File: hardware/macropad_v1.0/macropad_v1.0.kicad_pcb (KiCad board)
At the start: 2 copper layers, 61.9 x 76.2 mm, 50 parts, among them J1 USB_C_Receptacle_USB2.0_14P, SW1 SW_Push, SW2 Rotary Encoder, SW3 Rotary Encoder, U1 USBLC6-2SC6, U2 STM32F072C8T6, U3 XC6206PxxxMR

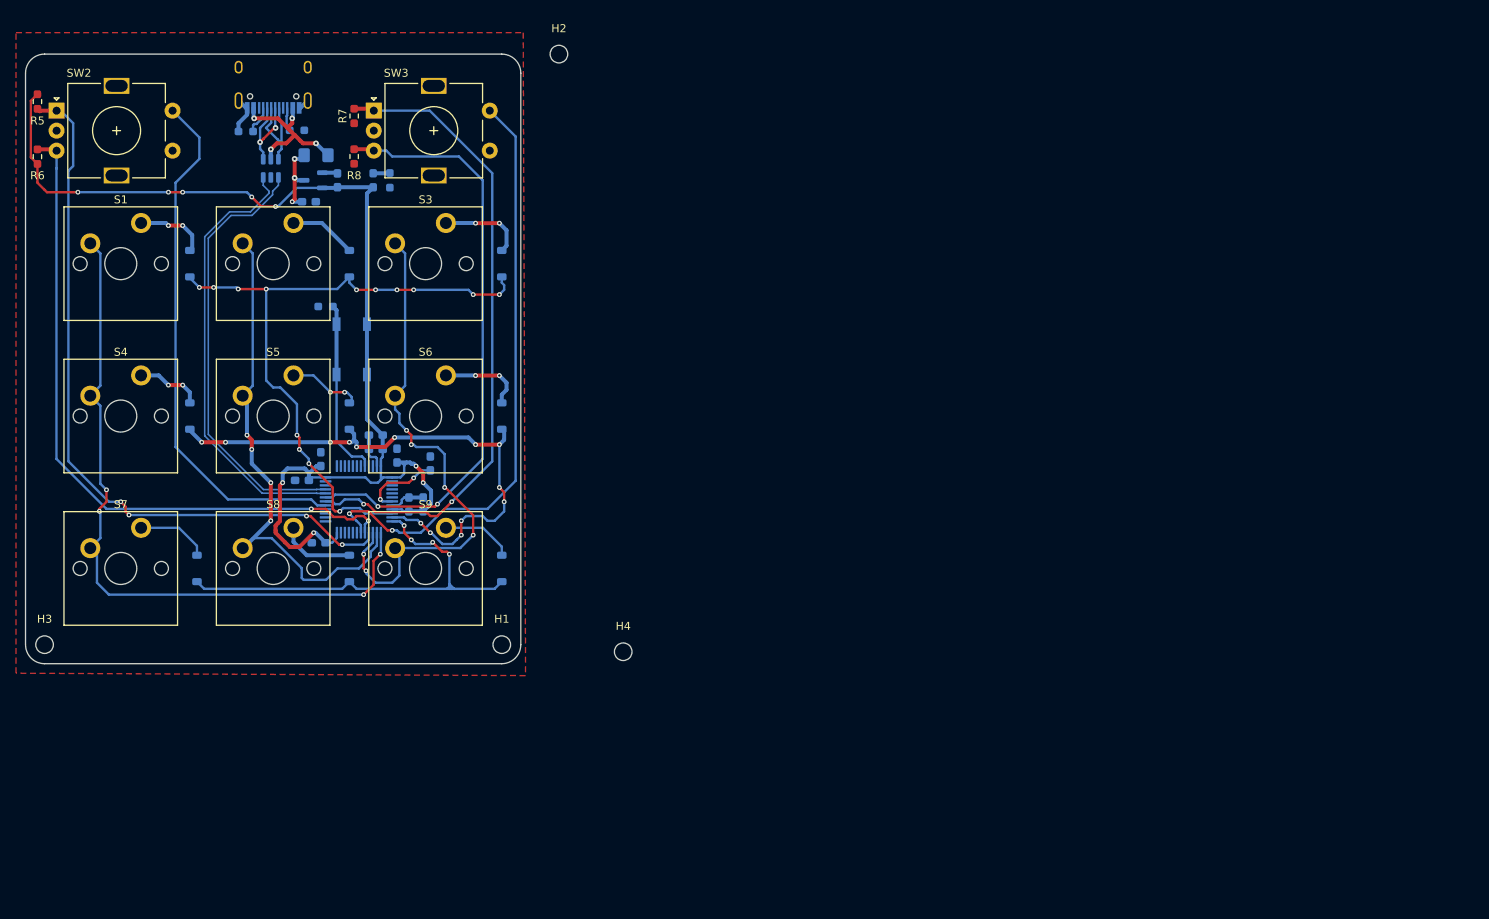
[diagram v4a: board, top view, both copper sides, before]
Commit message: Deleted old routing, redoing routing
-Rotated MCU so that datalines are facing upwards towards USB-C receptacle

-Made sure decoupling capacitors were routed to correct pins on MCU (they weren't before)

-Corrected minimum via sizing to match JLCPCB rules

-Cleaned up routing for USB-C receptacle to ESD protection unit to avoid interference from 5V line

-Next steps should be routing voltage step down so that I can route all the Vdd pins (3.3V)
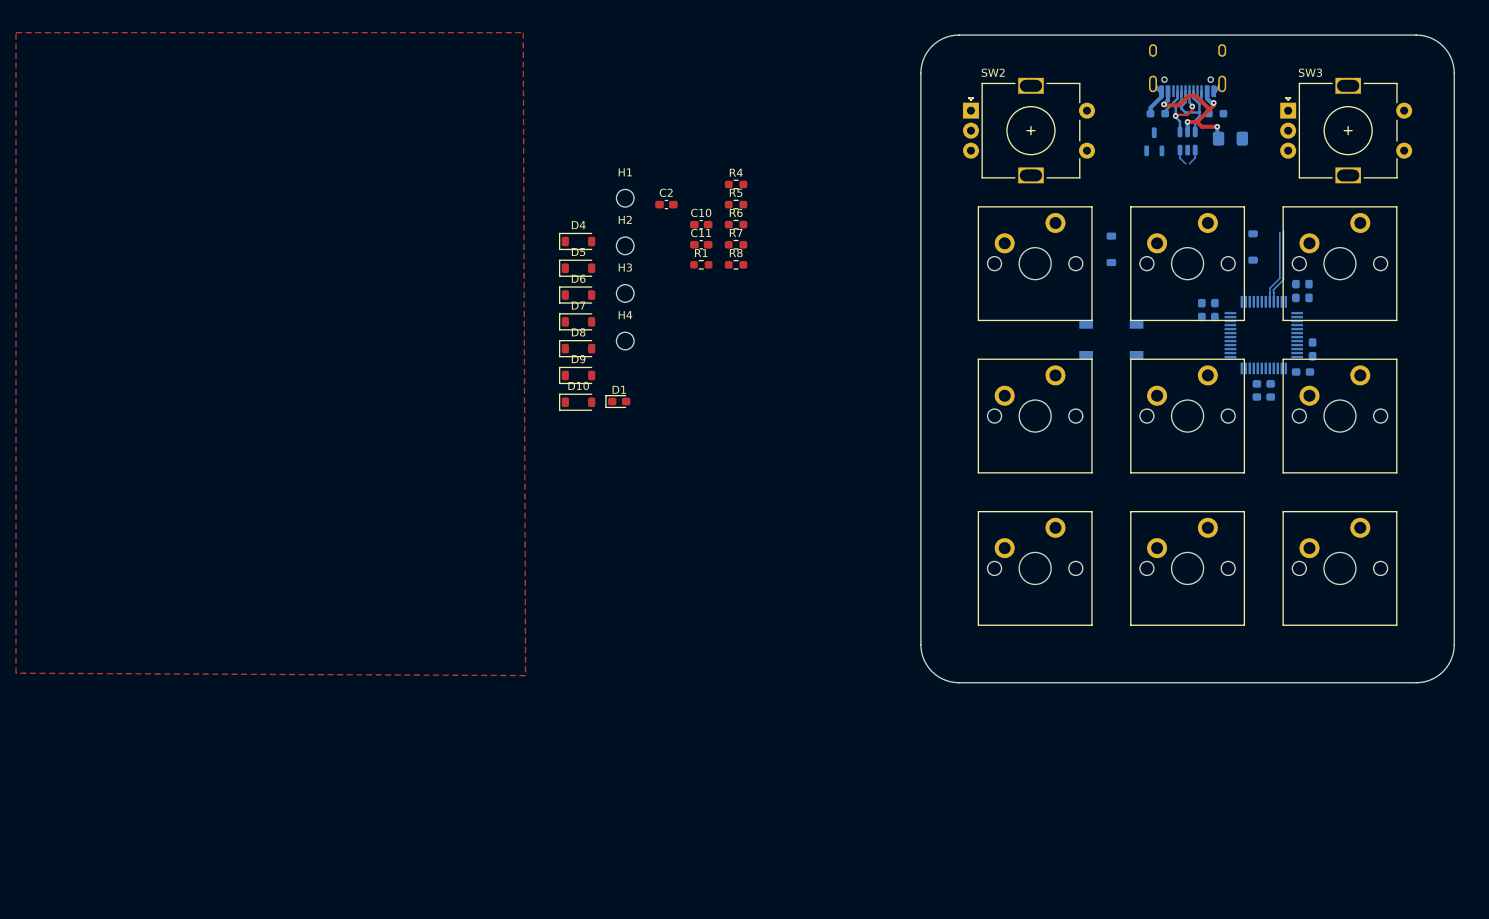
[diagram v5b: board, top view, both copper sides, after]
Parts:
- C10, C11, C2, D1, D10, D4, D5, D6, D7, D8, D9, R1, R4: moved to F.Cu
- moved C5 126.6 mm to (215.7, 58.3), turned to 90 degrees
- moved D2 115.2 mm to (190.5, 45.8)
- moved U2 115.0 mm to (209.6, 56.6), turned to 90 degrees
- moved R3 114.9 mm to (203.6, 28.9)
- moved U1 114.6 mm to (200.0, 32.3)
- moved C4 114.5 mm to (201.8, 53.4), turned to -90 degrees
- moved J1 114.3 mm to (200.0, 22.0)
- moved F1 114.3 mm to (205.4, 32.0), turned to 0 degrees
- moved S2 114.3 mm to (200.0, 47.6)
- moved S5 114.3 mm to (200.0, 66.7)
- moved S8 114.3 mm to (200.0, 85.7)
- moved S1 114.3 mm to (181.0, 47.6)
- moved S4 114.3 mm to (181.0, 66.7)
- moved S7 114.3 mm to (181.0, 85.7)
- moved SW3 114.3 mm to (212.6, 28.5)
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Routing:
- net VBAT: track 148.6 -> 0.00 mm, vias 9 -> 0
- net RENC_A1: track 91.1 -> 0.00 mm, vias 4 -> 0
- net COL_0: track 88.2 -> 0.00 mm, vias 4 -> 0
- net RENC_B1: track 85.2 -> 0.00 mm, vias 2 -> 0
- net ROW_0: track 83.4 -> 0.00 mm, vias 14 -> 0
- net RENC_A2: track 81.5 -> 0.00 mm, vias 2 -> 0
- net RENC_B2: track 75.4 -> 0.00 mm, vias 2 -> 0
- net RENC_SW2: track 75.3 -> 0.00 mm, vias 2 -> 0
- net ROW_1: track 72.2 -> 0.00 mm, vias 14 -> 0
- net COL_2: track 69.0 -> 0.00 mm, vias 6 -> 0
- net RENC_SW1: track 66.4 -> 0.00 mm
- net COL_1: track 66.0 -> 0.00 mm, vias 4 -> 0
- net ROW_2: track 55.2 -> 0.00 mm, vias 4 -> 0
- net USB_D-: track 55.6 -> 11.2 mm
- net USB_D+: track 54.8 -> 11.4 mm
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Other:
- board size 61.9 x 76.2 mm -> 66.7 x 81 mm

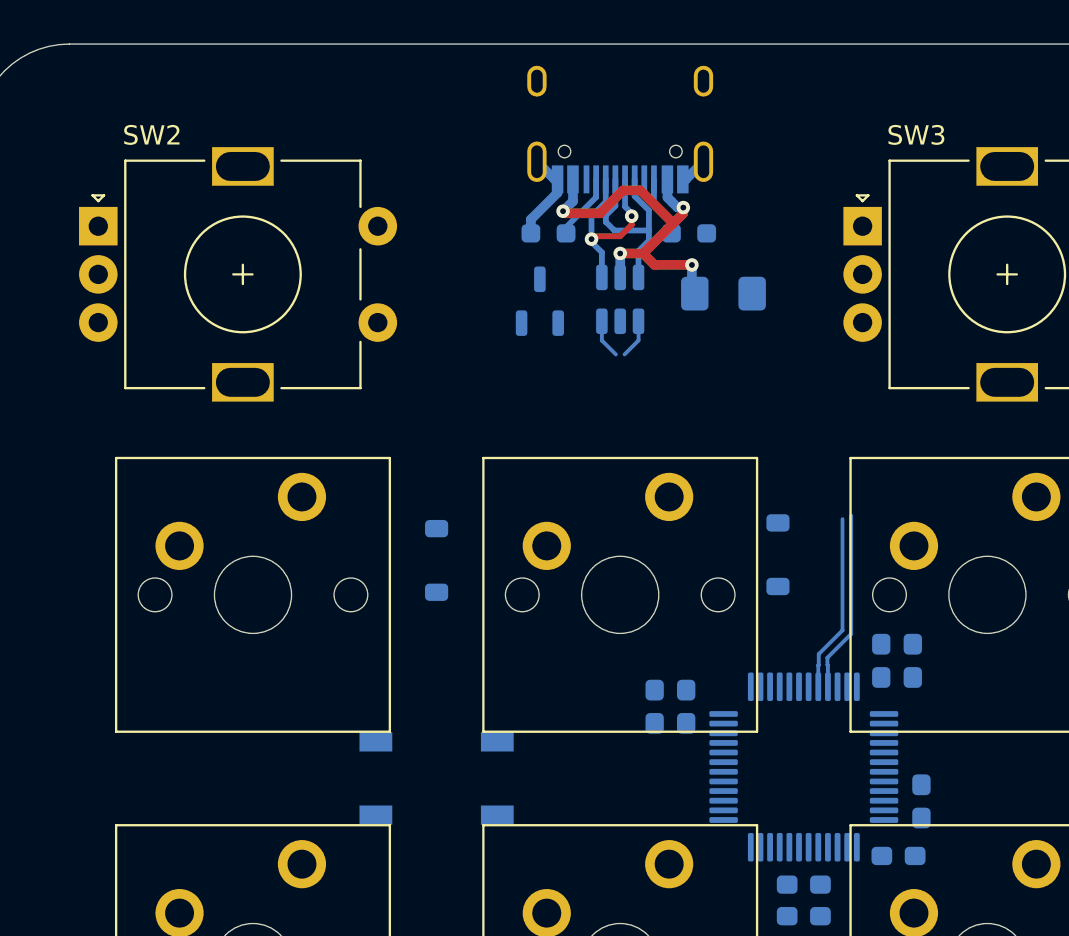
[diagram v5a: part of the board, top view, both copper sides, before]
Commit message: Routed voltage step down
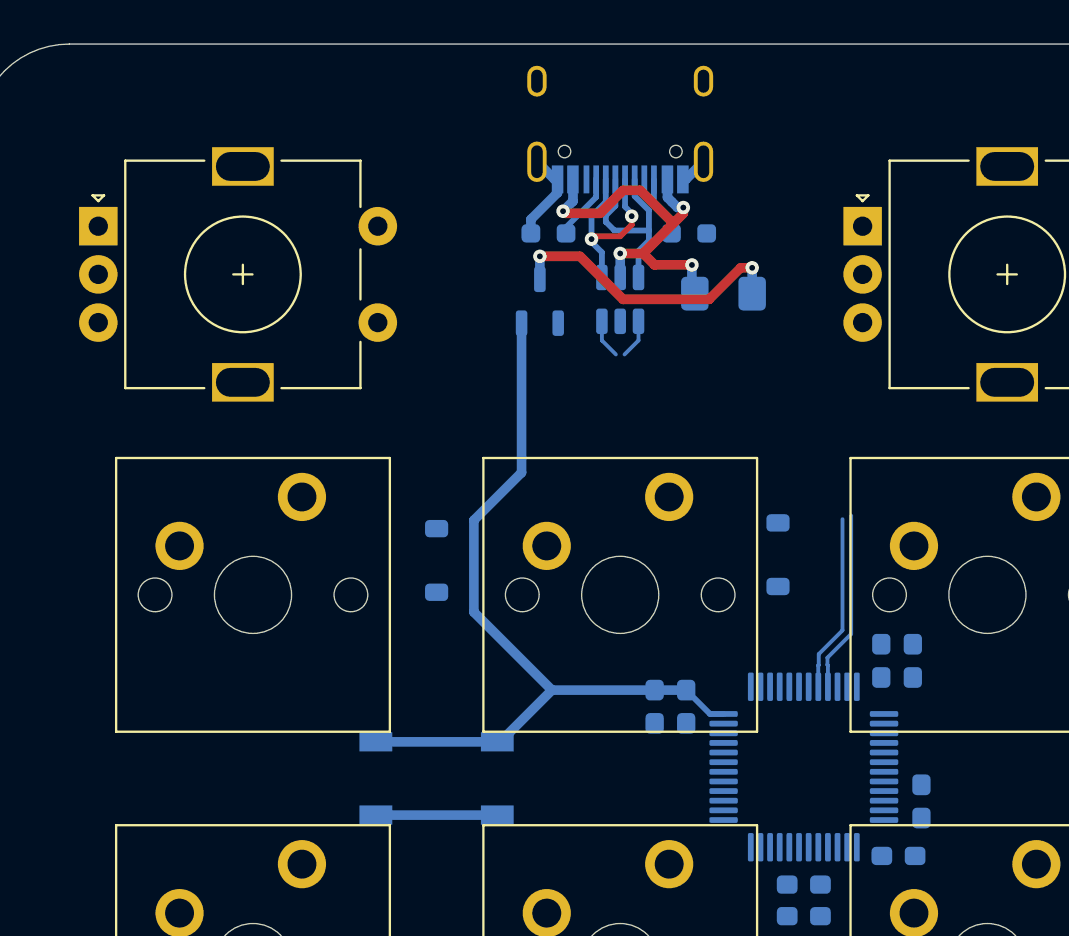
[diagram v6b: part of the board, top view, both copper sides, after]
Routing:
- net VBAT: track 0.00 -> 41.4 mm
- net +5V: track 0.00 -> 15.1 mm, vias 0 -> 2
- net BOOT0: track 0.00 -> 6.30 mm
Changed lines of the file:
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@@
 			(at 2.8 -4.7 0)
 			(layer "F.SilkS")
+			(hide yes)
 			(effects
 				(font
@@
 			(at 2.8 -4.7 0)
 			(layer "F.SilkS")
+			(hide yes)
 			(effects
 				(font
@@
 	)
 	(segment
+		(start 193.800228 55.249952)
+		(end 196.483428 52.566752)
+		(width 0.5)
+		(layer "B.Cu")
+		(net 1)
+	)
+	(segment
+		(start 201.810768 52.566752)
+		(end 203.447876 52.566752)
+		(width 0.5)
+		(layer "B.Cu")
+		(net 1)
+	)
+	(segment
+		(start 205.387676 53.804735)
+		(end 204.685859 53.804735)
+		(width 0.3)
+		(layer "B.Cu")
+		(net 1)
+	)
+	(segment
+		(start 204.685859 53.804735)
+		(end 203.447876 52.566752)
+		(width 0.3)
+		(layer "B.Cu")
+		(net 1)
+	)
+	(segment
+		(start 193.64984 55.249952)
+		(end 187.34984 55.249952)
+		(width 0.5)
+		(layer "B.Cu")
+		(net 1)
+	)
+	(segment
+		(start 192.434604 48.517928)
+		(end 196.483428 52.566752)
+		(width 0.5)
+		(layer "B.Cu")
+		(net 1)
+	)
+	(segment
+		(start 194.907648 33.52888)
+		(end 194.907648 41.282388)
+		(width 0.5)
+		(layer "B.Cu")
+		(net 1)
+	)
+	(segment
+		(start 196.483428 52.566752)
+		(end 201.810768 52.566752)
+		(width 0.5)
+		(layer "B.Cu")
+		(net 1)
+	)
+	(segment
+		(start 192.434604 43.755432)
+		(end 192.434604 48.517928)
+		(width 0.5)
+		(layer "B.Cu")
+		(net 1)
+	)
+	(segment
+		(start 194.907648 41.282388)
+		(end 192.434604 43.755432)
+		(width 0.5)
+		(layer "B.Cu")
+		(net 1)
+	)
+	(segment
+		(start 193.64984 55.249952)
+		(end 193.800228 55.249952)
+		(width 0.5)
+		(layer "B.Cu")
+		(net 1)
+	)
+	(segment
 		(start 203.275168 26.071581)
 		(end 203.430168 26.071581)
@@
 	)
 	(segment
+		(start 206.275608 30.658568)
+		(end 204.6385 32.295676)
+		(width 0.5)
+		(layer "F.Cu")
+		(net 4)
+	)
+	(segment
+		(start 204.6385 32.295676)
+		(end 200.17366 32.295676)
+		(width 0.5)
+		(layer "F.Cu")
+		(net 4)
+	)
+	(segment
+		(start 206.87092 30.658568)
+		(end 206.275608 30.658568)
+		(width 0.5)
+		(layer "F.Cu")
+		(net 4)
+	)
+	(segment
+		(start 200.17366 32.295676)
+		(end 197.94124 30.063256)
+		(width 0.5)
+		(layer "F.Cu")
+		(net 4)
+	)
+	(segment
+		(start 197.94124 30.063256)
+		(end 195.857648 30.063256)
+		(width 0.5)
+		(layer "F.Cu")
+		(net 4)
+	)
+	(via
+		(at 206.87092 30.658568)
+		(size 0.7)
+		(drill 0.3)
+		(layers "F.Cu" "B.Cu")
+		(net 4)
+	)
+	(via
+		(at 195.857648 30.063256)
+		(size 0.7)
+		(drill 0.3)
+		(layers "F.Cu" "B.Cu")
+		(net 4)
+	)
+	(segment
+		(start 206.87014 30.659348)
+		(end 206.87092 30.658568)
+		(width 0.5)
+		(layer "B.Cu")
+		(net 4)
+	)
+	(segment
+		(start 195.857648 30.063256)
+		(end 195.857648 31.25388)
+		(width 0.5)
+		(layer "B.Cu")
+		(net 4)
+	)
+	(segment
+		(start 206.87014 31.99802)
+		(end 206.87014 30.659348)
+		(width 0.5)
+		(layer "B.Cu")
+		(net 4)
+	)
+	(segment
 		(start 202.77815 28.351734)
 		(end 201.215456 29.914428)
@@
 	)
 	(segment
+		(start 187.34984 59.049952)
+		(end 193.64984 59.049952)
+		(width 0.5)
+		(layer "B.Cu")
+		(net 23)
+	)
+	(segment

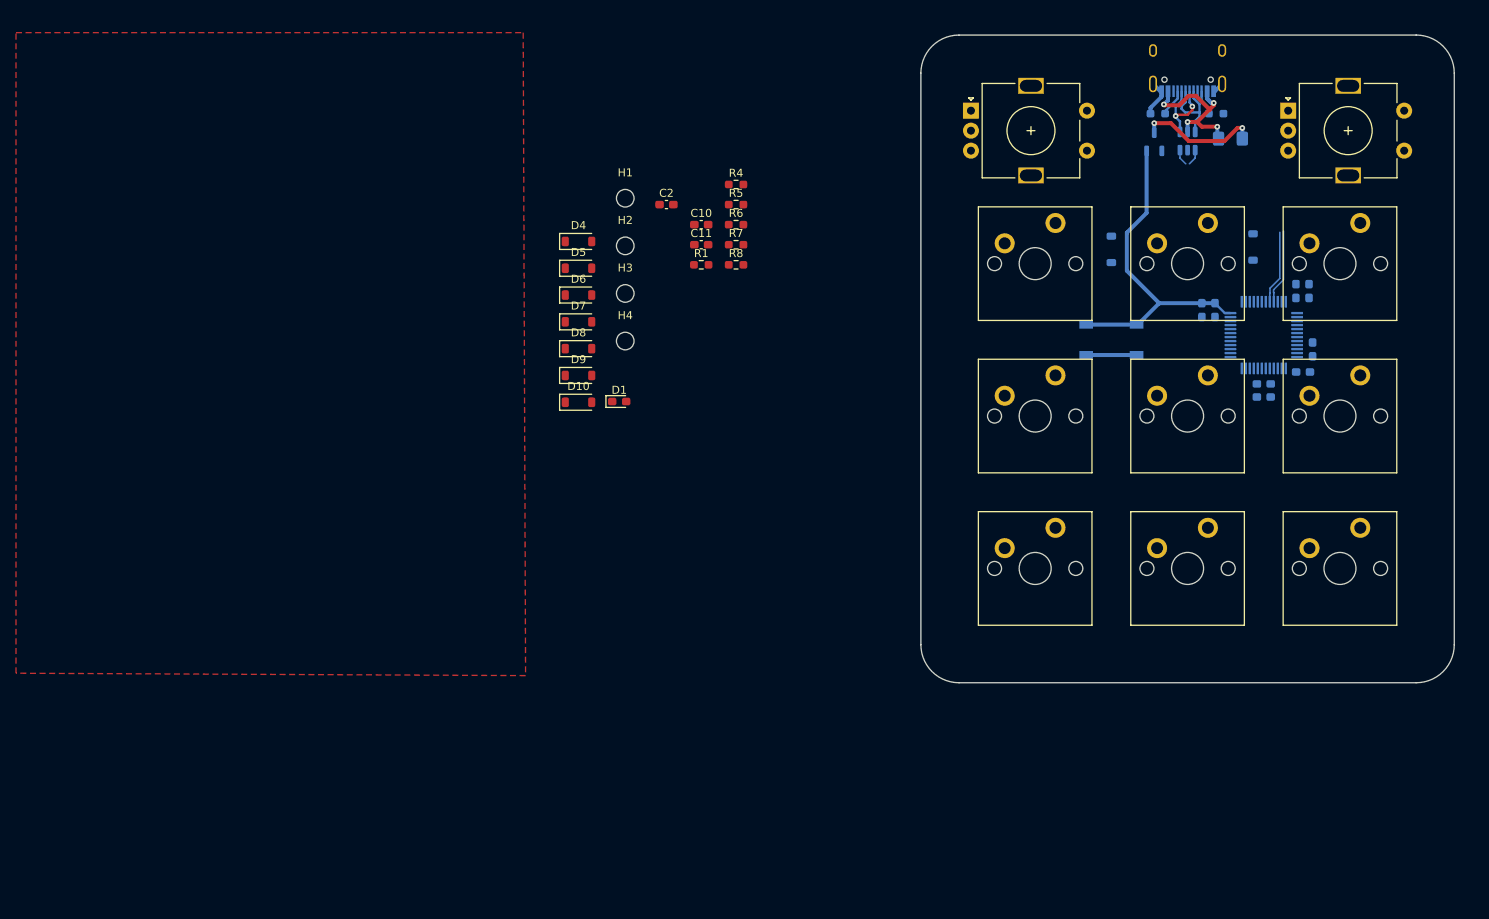
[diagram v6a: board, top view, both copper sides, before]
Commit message: Finished PCB design
-Routed everything

-Added a gnd plane to top layer

Next Steps:

-Make sure traces are wide enough

-Move all the silkscreen stuff

-Check for interference around voltage line

-Check that ground plane is fine

-Resolve the rest of the DRC errors/warnings
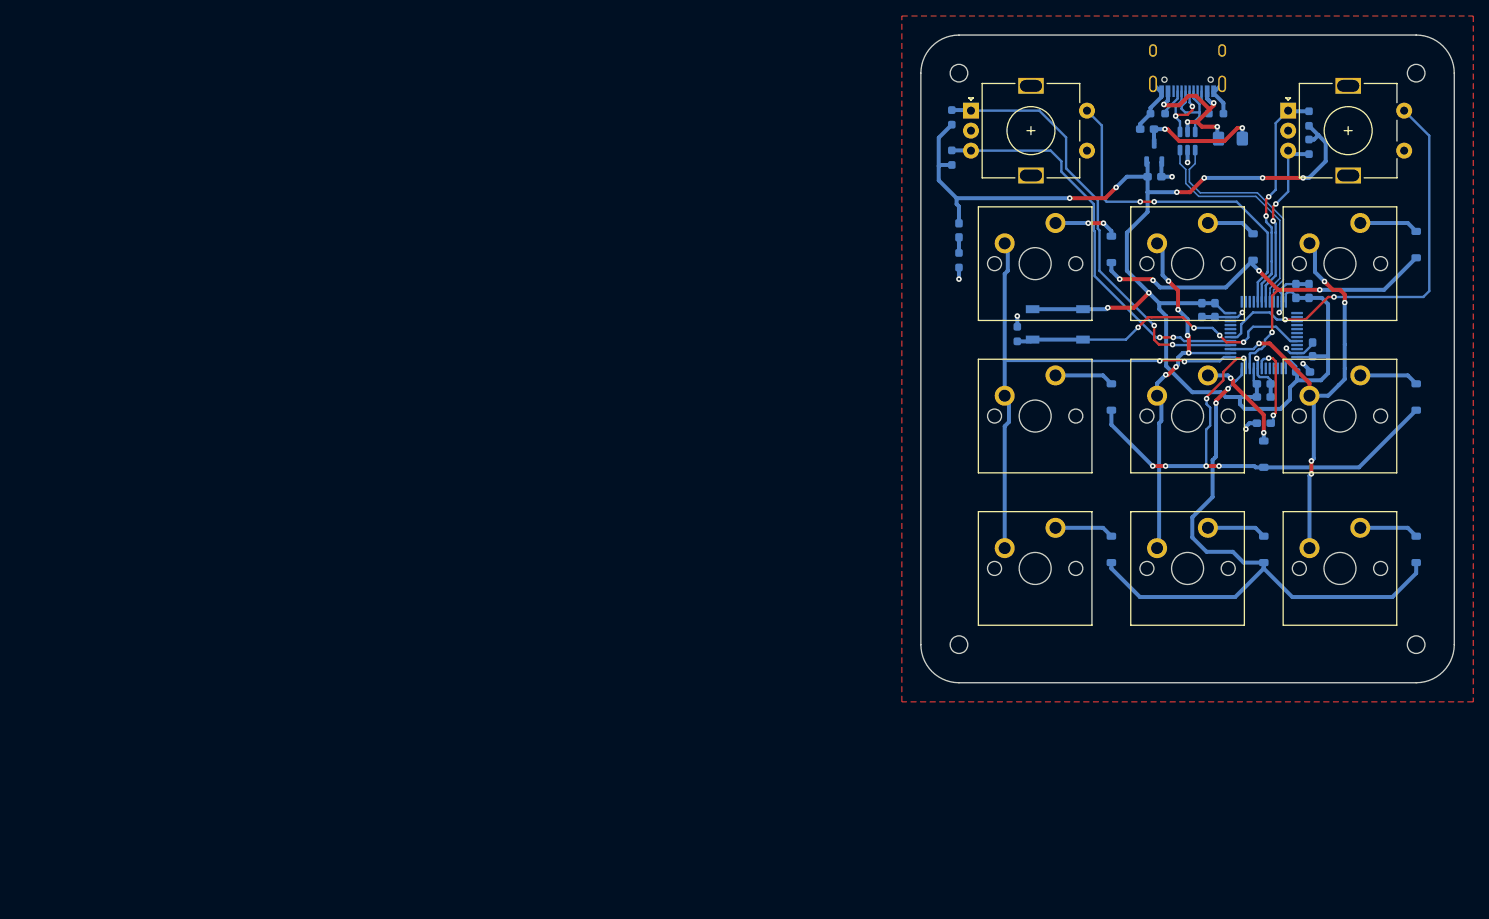
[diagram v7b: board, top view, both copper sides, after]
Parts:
- C10, C11, C2, D1, D10, D4, D5, D6, D7, D8, D9, R1, R4, R5, R6, R7, R8: moved to B.Cu
- moved H2 110.7 mm to (228.6, 95.2)
- moved D10 106.3 mm to (228.6, 83.3), turned to 90 degrees
- moved D7 105.1 mm to (228.6, 64.3), turned to 90 degrees
- moved D4 104.7 mm to (228.6, 45.2), turned to 90 degrees
- moved H4 104.4 mm to (228.6, 23.8)
- moved D9 88.4 mm to (209.6, 83.3), turned to 90 degrees
- moved D6 87.9 mm to (209.6, 71.4), turned to 90 degrees
- moved C2 79.5 mm to (209.5, 67.6)
- moved R7 73.3 mm to (215.2, 29.5), turned to 90 degrees
- moved R8 73.1 mm to (215.2, 33.0), turned to -90 degrees
- moved D8 71.2 mm to (190.5, 83.3), turned to 90 degrees
- moved H1 69.7 mm to (171.4, 95.2)
- moved D5 68.5 mm to (190.5, 64.3), turned to 90 degrees
- moved C11 57.3 mm to (195.9, 36.8)
- moved C10 57.0 mm to (195.0, 30.8), turned to 180 degrees
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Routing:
- net VBAT: track 41.4 -> 180.2 mm, vias 0 -> 8
- net ROW_2: track 0.00 -> 81.2 mm, vias 0 -> 2
- net COL_0: track 0.00 -> 67.5 mm, vias 0 -> 2
- net ROW_1: track 0.00 -> 62.7 mm, vias 0 -> 6
- net COL_2: track 0.00 -> 57.9 mm, vias 0 -> 5
- net ROW_0: track 0.00 -> 56.7 mm, vias 0 -> 5
- net RENC_A1: track 0.00 -> 55.4 mm, vias 0 -> 2
- net RENC_SW2: track 0.00 -> 52.5 mm, vias 0 -> 2
- net RENC_B1: track 0.00 -> 50.7 mm, vias 0 -> 2
- net COL_1: track 0.00 -> 47.7 mm, vias 0 -> 6
- net RENC_SW1: track 0.00 -> 43.3 mm, vias 0 -> 2
- net GND: track 6.27 -> 45.5 mm, vias 0 -> 10
- net BOOT0: track 6.30 -> 39.5 mm, vias 0 -> 4
- net RENC_A2: track 0.00 -> 28.5 mm, vias 0 -> 2
- net RENC_B2: track 0.00 -> 23.1 mm, vias 0 -> 2
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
